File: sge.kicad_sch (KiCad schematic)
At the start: 27 parts, among them IC6 315-5660

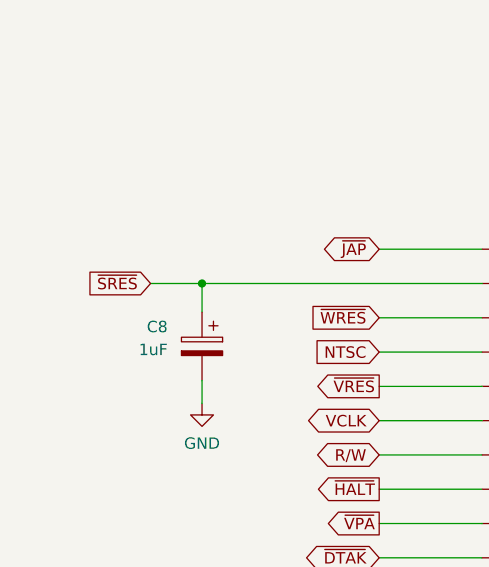
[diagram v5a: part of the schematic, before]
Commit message: Use 32X reset(s) for MD side.
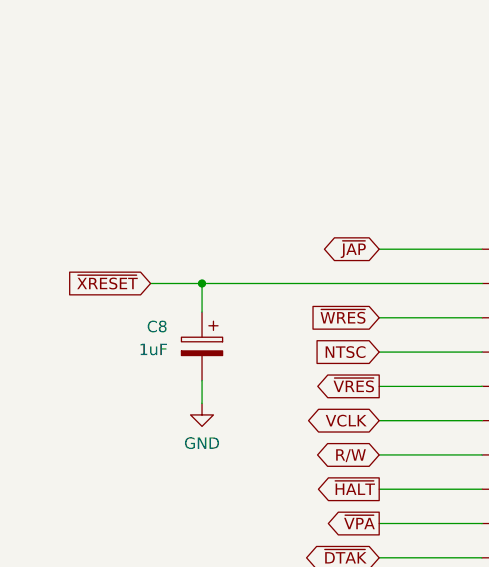
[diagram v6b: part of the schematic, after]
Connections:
- net ~{SRES} renamed ~{XRESET}
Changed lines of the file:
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@@
-    )
-  )
-  (global_label "~{SRES}" (shape input) (at 25.4 64.77 180) (fields_autoplaced)
-    (effects (font (size 1.27 1.27)) (justify right))
-    (property "Intersheetrefs" "${INTERSHEET_REFS}" (at 17.5768 64.77 0)
-      (effects (font (size 1.27 1.27)) (justify right) hide)
     )
   )
@@
       (effects (font (size 1.27 1.27)) (justify right) hide)
     )
+  )
+  (global_label "~{XRESET}" (shape input) (at 25.4 64.77 180) (fields_autoplaced)
+    (effects (font (size 1.27 1.27)) (justify right))
+    (property "Intersheetrefs" "${INTERSHEET_REFS}" (at 15.4602 64.77 0)
+      (effects (font (size 1.27 1.27)) (justify right) hide)
+    )

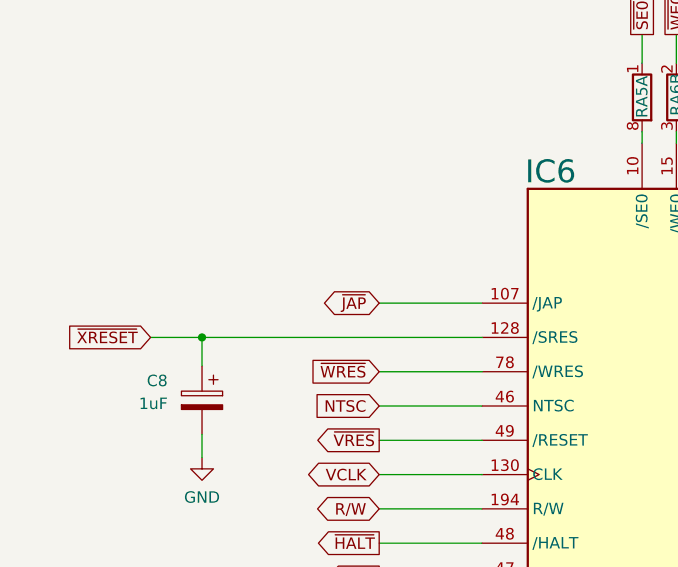
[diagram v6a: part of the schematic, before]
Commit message: Remove mono audio, switch to 2-unit opamp.
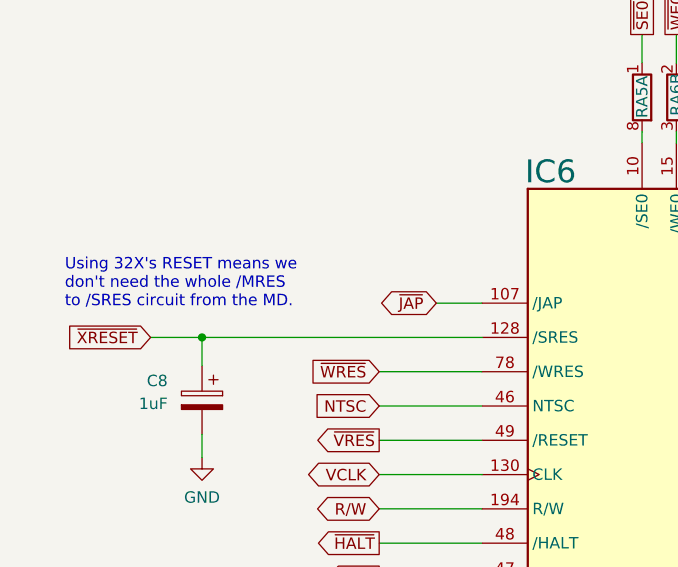
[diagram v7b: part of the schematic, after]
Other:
- note added: "Using 32X's RESET means we don't need the whole /MRES to /SRES circuit from the MD."
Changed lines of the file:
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@@
     (stroke (width 0) (type default))
   )
-  (wire (pts (xy 50.8 60.96) (xy 62.23 60.96))
+  (wire (pts (xy 57.15 60.96) (xy 62.23 60.96))
     (stroke (width 0) (type default))
   )
@@
   )
   (text "PAL\nONLY" (at 398.145 74.295 0)
+    (effects (font (size 1.27 1.27)) (justify left bottom))
+  )
+  (text "Using 32X's RESET means we\ndon't need the whole /MRES\nto /SRES circuit from the MD."
+    (at 15.875 61.595 0)
     (effects (font (size 1.27 1.27)) (justify left bottom))
   )
@@
     )
   )
-  (global_label "~{JAP}" (shape bidirectional) (at 50.8 60.96 180) (fields_autoplaced)
-    (effects (font (size 1.27 1.27)) (justify right))
-    (property "Intersheetrefs" "${INTERSHEET_REFS}" (at 43.3773 60.96 0)
-      (effects (font (size 1.27 1.27)) (justify right) hide)
-    )
+  (global_label "~{JAP}" (shape bidirectional) (at 57.15 60.96 180) (fields_autoplaced)
+    (effects (font (size 1.27 1.27)) (justify right))
+    (property "Intersheetrefs" "${INTERSHEET_REFS}" (at 49.7273 60.96 0)
+      (effects (font (size 1.27 1.27)) (justify right) hide)
+    )

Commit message: Added LCSC Part # for some of the bird seed
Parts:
- C1: LCSC Part # (none) -> C2224419
- C1: LCSC Part # (none) -> C2237538
- C2: LCSC Part # (none) -> C2232461
- C8: LCSC Part # (none) -> C1850591
- FB7: LCSC Part # (none) -> C2441367
- R3: LCSC Part # (none) -> C3008897
- R3: LCSC Part # (none) -> C2077067
- R3: LCSC Part # (none) -> C313845
- RA1, RA2, RA3, RA4, RA5: LCSC Part # (none) -> C136838
- RA6: LCSC Part # (none) -> C728824
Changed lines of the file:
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@@
+      (effects (font (size 1.27 1.27)) hide)
+    )
+    (property "LCSC Part #" "C136838" (at 113.03 38.1 0)
       (effects (font (size 1.27 1.27)) hide)
     )
@@
     )
     (property "DigiKey" "" (at 213.36 130.81 0)
+      (effects (font (size 1.27 1.27)) hide)
+    )
+    (property "LCSC Part #" "" (at 213.36 130.81 0)
       (effects (font (size 1.27 1.27)) hide)
     )
@@
       (effects (font (size 1.27 1.27)) hide)
     )
+    (property "LCSC Part #" "C3008897" (at 139.7 256.54 0)
+      (effects (font (size 1.27 1.27)) hide)
+    )
     (pin "1")
     (pin "2")
@@
       (effects (font (size 1.27 1.27)) hide)
     )
+    (property "LCSC Part #" "C136838" (at 99.06 38.1 0)
+      (effects (font (size 1.27 1.27)) hide)
+    )
     (pin "1")
     (pin "8")
@@
       (effects (font (size 1.27 1.27)) hide)
     )
+    (property "LCSC Part #" "C136838" (at 124.46 38.1 0)
+      (effects (font (size 1.27 1.27)) hide)
+    )
     (pin "1")
     (pin "8")
@@
       (effects (font (size 1.27 1.27)) hide)
     )
+    (property "LCSC Part #" "C136838" (at 116.84 38.1 0)
+      (effects (font (size 1.27 1.27)) hide)
+    )
     (pin "1")
     (pin "8")
@@
     )
     (property "DigiKey" "" (at 264.16 238.125 0)
+      (effects (font (size 1.27 1.27)) hide)
+    )
+    (property "LCSC Part #" "" (at 264.16 238.125 0)
       (effects (font (size 1.27 1.27)) hide)
     )
@@
       (effects (font (size 1.27 1.27)) hide)
     )
+    (property "LCSC Part #" "C136838" (at 198.12 38.1 0)
+      (effects (font (size 1.27 1.27)) hide)
+    )
     (pin "1")
     (pin "8")
@@
       (effects (font (size 1.27 1.27)) hide)
     )
+    (property "LCSC Part #" "C2232461" (at 261.62 260.985 0)
+      (effects (font (size 1.27 1.27)) hide)
+    )
     (pin "1")
     (pin "2")
@@
       (effects (font (size 1.27 1.27)) hide)
     )
+    (property "LCSC Part #" "C728824" (at 106.68 38.1 0)
+      (effects (font (size 1.27 1.27)) hide)
+    )
     (pin "1")
     (pin "4")
@@
       (effects (font (size 1.27 1.27)) hide)
     )
+    (property "LCSC Part #" "C3008897" (at 392.43 52.07 0)
+      (effects (font (size 1.27 1.27)) hide)
+    )
     (pin "1")
     (pin "2")
@@
       (effects (font (size 1.27 1.27)) hide)
     )
+    (property "LCSC Part #" "C2224419" (at 175.26 264.16 0)
+      (effects (font (size 1.27 1.27)) hide)
+    )
     (pin "1")
     (pin "2")
@@
       (effects (font (size 1.27 1.27)) hide)
     )
+    (property "LCSC Part #" "C1850591" (at 30.48 174.625 0)
+      (effects (font (size 1.27 1.27)) hide)
+    )
     (pin "1")
     (pin "2")
@@
       (effects (font (size 1.27 1.27)) hide)
     )
+    (property "LCSC Part #" "C2224419" (at 160.655 264.16 0)
+      (effects (font (size 1.27 1.27)) hide)
+    )
     (pin "1")
     (pin "2")
@@
       (effects (font (size 1.27 1.27)) hide)
     )
+    (property "LCSC Part #" "C2224419" (at 295.275 238.125 0)
+      (effects (font (size 1.27 1.27)) hide)
+    )
     (pin "1")
     (pin "2")
@@
       (effects (font (size 1.27 1.27)) hide)
     )
+    (property "LCSC Part #" "C136838" (at 135.89 38.1 0)
+      (effects (font (size 1.27 1.27)) hide)
+    )
     (pin "1")
     (pin "8")
@@
       (effects (font (size 1.27 1.27)) hide)
     )
+    (property "LCSC Part #" "C728824" (at 83.82 38.1 0)
+      (effects (font (size 1.27 1.27)) hide)
+    )
     (pin "1")
     (pin "4")
@@
       (effects (font (size 1.27 1.27)) hide)
     )
+    (property "LCSC Part #" "C136838" (at 120.65 38.1 0)
+      (effects (font (size 1.27 1.27)) hide)
+    )
     (pin "1")
     (pin "8")
@@
       (effects (font (size 1.27 1.27)) hide)
     )
+    (property "LCSC Part #" "C136838" (at 179.07 38.1 0)
+      (effects (font (size 1.27 1.27)) hide)
+    )
     (pin "1")
     (pin "8")
@@
       (effects (font (size 1.27 1.27)) hide)
     )
+    (property "LCSC Part #" "C3008897" (at 354.33 229.87 0)
+      (effects (font (size 1.27 1.27)) hide)
+    )
     (pin "1")
     (pin "2")
@@
       (effects (font (size 1.27 1.27)) hide)
     )
+    (property "LCSC Part #" "C136838" (at 132.08 38.1 0)
+      (effects (font (size 1.27 1.27)) hide)
+    )
     (pin "1")
     (pin "8")
@@
       (effects (font (size 1.27 1.27)) hide)
     )
+    (property "LCSC Part #" "" (at 127 256.54 0)
+      (effects (font (size 1.27 1.27)) hide)
+    )
     (pin "1")
     (pin "2")
@@
       (effects (font (size 1.27 1.27)) hide)
     )
+    (property "LCSC Part #" "C136838" (at 201.93 38.1 0)
+      (effects (font (size 1.27 1.27)) hide)
+    )
     (pin "1")
     (pin "8")
@@
     )
     (property "DigiKey" "" (at 321.31 238.125 0)
+      (effects (font (size 1.27 1.27)) hide)
+    )
+    (property "LCSC Part #" "C2224419" (at 321.31 238.125 0)
       (effects (font (size 1.27 1.27)) hide)
     )
@@
       (effects (font (size 1.27 1.27)) hide)
     )
+    (property "LCSC Part #" "C136838" (at 194.31 38.1 0)
+      (effects (font (size 1.27 1.27)) hide)
+    )
     (pin "1")
     (pin "8")
@@
       (effects (font (size 1.27 1.27)) hide)
     )
+    (property "LCSC Part #" "C136838" (at 128.27 38.1 0)
+      (effects (font (size 1.27 1.27)) hide)
+    )
     (pin "1")
     (pin "8")
@@
       (effects (font (size 1.27 1.27)) hide)
     )
+    (property "LCSC Part #" "C136838" (at 102.87 38.1 0)
+      (effects (font (size 1.27 1.27)) hide)
+    )
     (pin "1")
     (pin "8")
@@
       (effects (font (size 1.27 1.27)) hide)
     )
+    (property "LCSC Part #" "C2077067" (at 390.525 195.58 0)
+      (effects (font (size 1.27 1.27)) hide)
+    )
     (pin "1")
     (pin "2")
@@
       (effects (font (size 1.27 1.27)) hide)
     )
+    (property "LCSC Part #" "C2224419" (at 314.96 238.125 0)
+      (effects (font (size 1.27 1.27)) hide)
+    )
     (pin "1")
     (pin "2")
@@
       (effects (font (size 1.27 1.27)) hide)
     )
+    (property "LCSC Part #" "C136838" (at 80.01 38.1 0)
+      (effects (font (size 1.27 1.27)) hide)
+    )
     (pin "1")
     (pin "8")
@@
     )
     (property "DigiKey" "" (at 252.73 254.635 0)
+      (effects (font (size 1.27 1.27)) hide)
+    )
+    (property "LCSC Part #" "C2441367" (at 252.73 254.635 0)
       (effects (font (size 1.27 1.27)) hide)
     )
@@
       (effects (font (size 1.27 1.27)) hide)
     )
+    (property "LCSC Part #" "C136838" (at 190.5 38.1 0)
+      (effects (font (size 1.27 1.27)) hide)
+    )
     (pin "1")
     (pin "8")
@@
       (effects (font (size 1.27 1.27)) hide)
     )
+    (property "LCSC Part #" "C136838" (at 139.7 38.1 0)
+      (effects (font (size 1.27 1.27)) hide)
+    )
     (pin "1")
     (pin "8")
@@
       (effects (font (size 1.27 1.27)) hide)
     )
+    (property "LCSC Part #" "C313845" (at 234.95 247.65 0)
+      (effects (font (size 1.27 1.27)) hide)
+    )
     (pin "1")
     (pin "2")
@@
       (effects (font (size 1.27 1.27)) hide)
     )
+    (property "LCSC Part #" "" (at 278.13 238.125 0)
+      (effects (font (size 1.27 1.27)) hide)
+    )
     (pin "1")
     (pin "2")
@@
       (effects (font (size 1.27 1.27)) hide)
     )
+    (property "LCSC Part #" "C136838" (at 205.74 38.1 0)
+      (effects (font (size 1.27 1.27)) hide)
+    )
     (pin "1")
     (pin "8")
@@
     )
     (property "DigiKey" "" (at 388.62 72.39 0)
+      (effects (font (size 1.27 1.27)) hide)
+    )
+    (property "LCSC Part #" "C2237538" (at 388.62 72.39 0)
       (effects (font (size 1.27 1.27)) hide)
     )
@@
       (effects (font (size 1.27 1.27)) hide)
     )
+    (property "LCSC Part #" "C136838" (at 95.25 38.1 0)
+      (effects (font (size 1.27 1.27)) hide)
+    )
     (pin "1")
     (pin "8")
@@
     )
     (property "DigiKey" "" (at 31.115 71.755 0)
+      (effects (font (size 1.27 1.27)) hide)
+    )
+    (property "LCSC Part #" "C1850591" (at 31.115 71.755 0)
       (effects (font (size 1.27 1.27)) hide)
     )
@@
       (effects (font (size 1.27 1.27)) hide)
     )
+    (property "LCSC Part #" "C2224419" (at 200.025 264.16 0)
+      (effects (font (size 1.27 1.27)) hide)
+    )
     (pin "1")
     (pin "2")
@@
       (effects (font (size 1.27 1.27)) hide)
     )
+    (property "LCSC Part #" "C136838" (at 186.69 38.1 0)
+      (effects (font (size 1.27 1.27)) hide)
+    )
     (pin "1")
     (pin "8")
@@
     )
     (property "DigiKey" "" (at 187.96 264.16 0)
+      (effects (font (size 1.27 1.27)) hide)
+    )
+    (property "LCSC Part #" "C2224419" (at 187.96 264.16 0)
       (effects (font (size 1.27 1.27)) hide)
     )
@@
       (effects (font (size 1.27 1.27)) hide)
     )
+    (property "LCSC Part #" "C136838" (at 182.88 38.1 0)
+      (effects (font (size 1.27 1.27)) hide)
+    )
